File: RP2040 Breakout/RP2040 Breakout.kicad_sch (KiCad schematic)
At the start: 46 parts, among them J1 USB_C_Receptacle_USB2.0, J3 Conn_01x16_Pin, J5 Conn_01x16_Pin, SW1 SW_Push, SW2 SW_Push, SW3 SW_Push, SW4 SW_Push, U1 RP2040, U3 W25Q128JVS, U4 LP2980IM5X-3.3, X1 ABM8G-12.000MHZ-B4Y-T

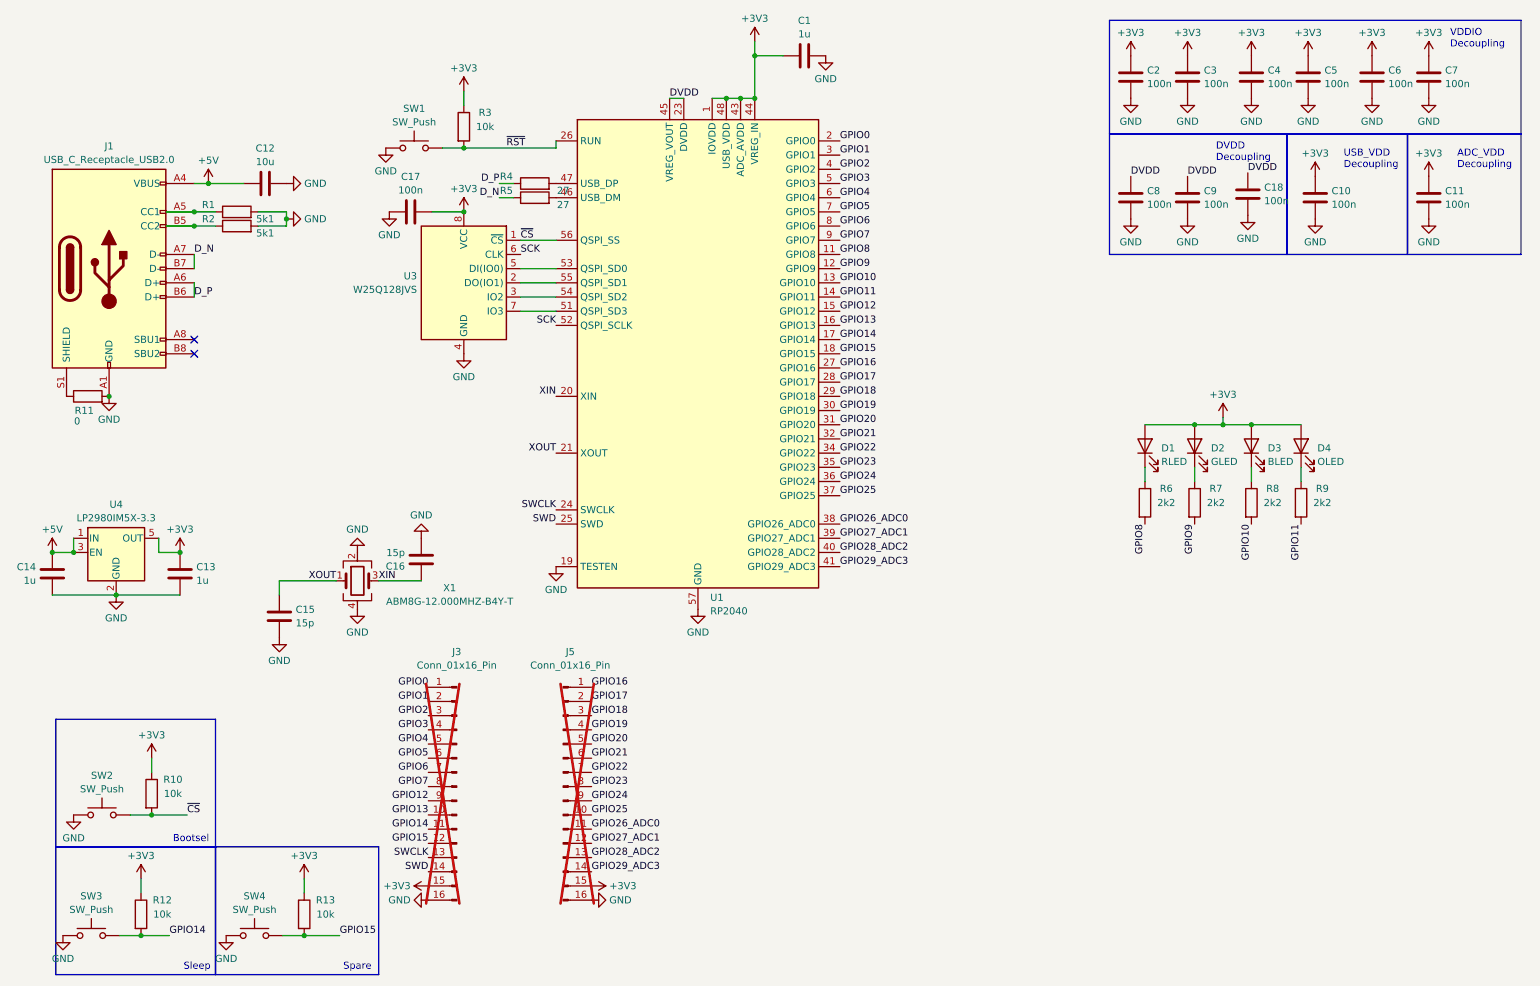
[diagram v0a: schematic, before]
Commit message: Cleaned up schematic a bit and rerouted buttons.
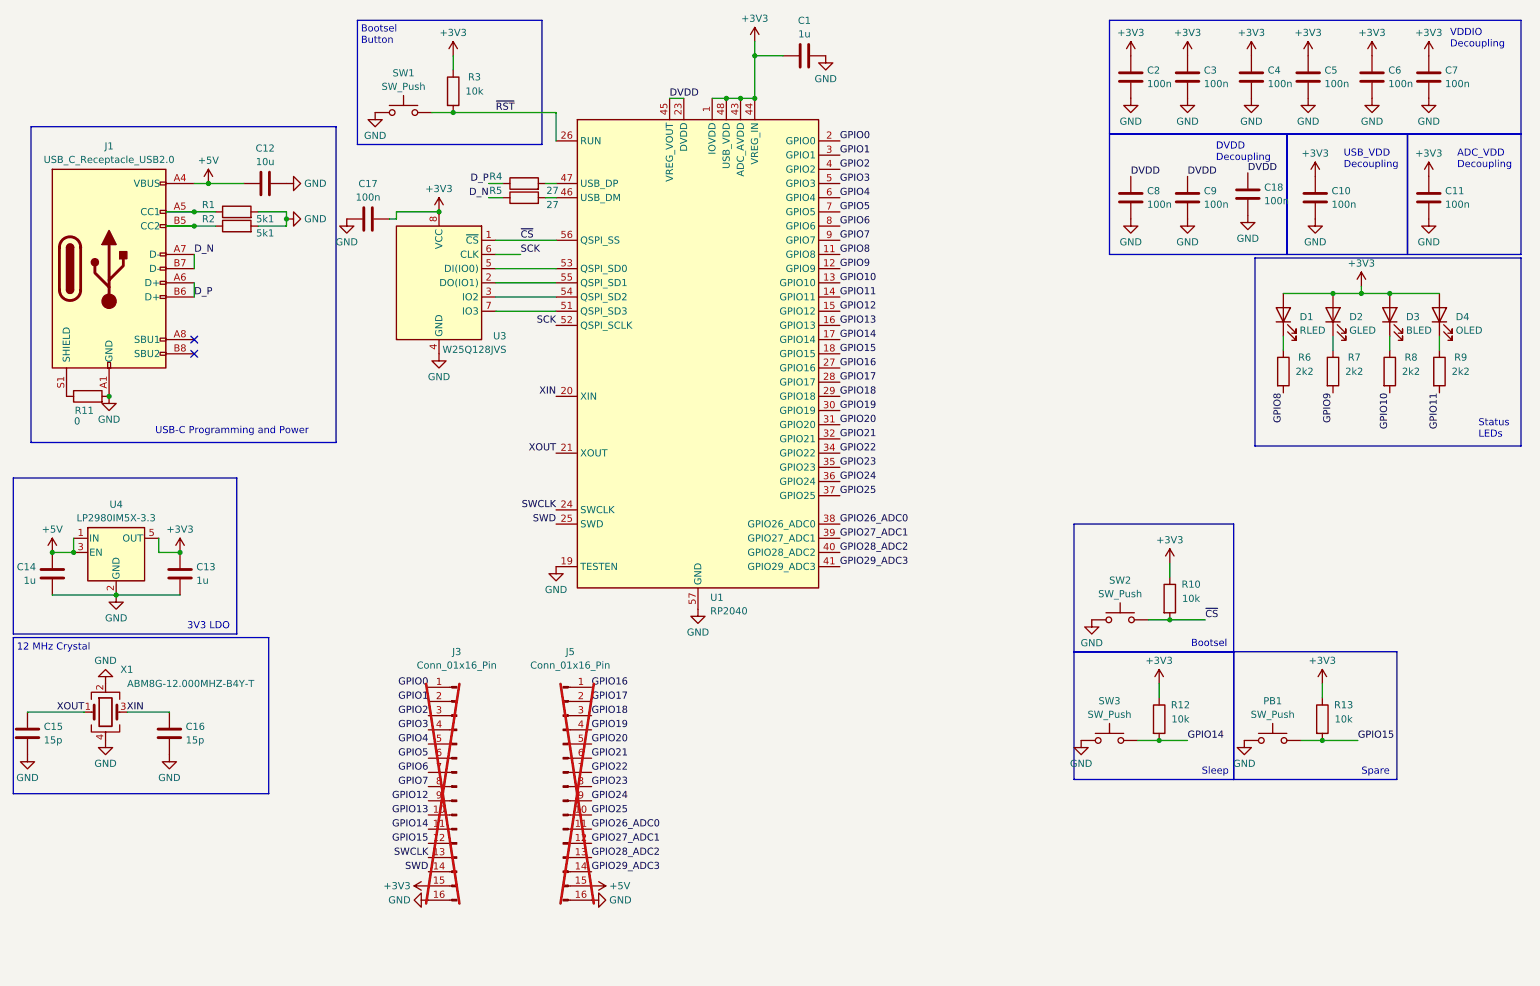
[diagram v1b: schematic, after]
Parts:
- R10, R11, R12, R13, R3, R4, R5, R6, R7, R8, R9: footprint R_0402_1005Metric -> Resistor_SMD:R_0402_1005Metric
- renumbered SW4 to PB1
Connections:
- net +3V3: no longer J5.15 (Pin_15)
- net +5V: now also J5.15 (Pin_15)
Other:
- note added: "12 MHz Crystal"
- note added: "3V3 LDO"
- note added: "Bootsel Button"
- note added: "Status LEDs"
- note added: "USB-C Programming and Power"
- moved on the sheet: C15, C16, C17, D1, D2, D3, D4, PB1, R10, R12, R13, R3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

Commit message: Add title block to schematic.
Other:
- company: (none) -> Tobias McKellar
- title: (none) -> RP2040 Breakout
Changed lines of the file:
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@@
 (kicad_sch (version 20230121) (generator eeschema)
   (paper "A4")
+  (title_block
+    (title "RP2040 Breakout")
+    (date "2024-06-03")
+    (rev "1")
+    (company "Tobias McKellar")
+  )
   (junction (at 43.18 109.22) (diameter 0) (color 0 0 0 0)
   )
